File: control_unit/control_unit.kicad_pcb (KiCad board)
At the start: 2 copper layers, 100 x 95 mm, 111 parts, among them J1 Conn_02x03_Counter_Clockwise, J2 Conn_01x02_Socket, J4 SERVO_PWM, J5 BLDC1, J6 BLDC1, J7 BLDC1, J8 BLDC1, J9 Barrel_Jack_Switch, M1 Motor_Servo, M2 Fan, Q3 2N7002, Q4 MMBT5551L, Q7 AO3400A, Q8 AO3400A, U14 MCP2515-xSO, U15 BNO055 DIP, U3 ATA6561-GAQW-N, U4 ADS1015IDGS, X1 16MHz

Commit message: control_unit Rev00発注
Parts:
- added G***: LOGO, myfootprint:aqua_logo, F.Cu at (167.5, 69.8)
- added LED2: GREEN, LED_SMD:LED_0805_2012Metric, F.Cu at (130.5, 115.2)
- added R16: 1.2k, Resistor_SMD:R_0603_1608Metric, F.Cu at (130.5, 119.6)
- Analog_IN1: footprint Connector_JST:JST_XH_B4B-XH-AM_1x04_P2.50mm_Vertical -> Connector_JST:JST_XA_B04B-XASK-1-A_1x04_P2.50mm_Vertical
- CAN1: footprint Connector_JST:JST_XH_B2B-XH-A_1x02_P2.50mm_Vertical -> Connector_JST:JST_XA_B02B-XASK-1-A_1x02_P2.50mm_Vertical
- D2: value ~ -> SS54
- J4: footprint Connector_JST:JST_XH_B4B-XH-A_1x04_P2.50mm_Vertical -> Connector_JST:JST_XA_B04B-XASK-1-A_1x04_P2.50mm_Vertical
- LED1, LED_BNO1, LED_ESC_1, LED_ESC_2, LED_ESC_3, LED_ESC_4: footprint LED_SMD:LED_1206_3216Metric -> LED_SMD:LED_0805_2012Metric
- moved C1 24.5 mm to (98.0, 76.1)
- moved C2 24.5 mm to (152.0, 77.1)
- moved C5 24.5 mm to (137.6, 89.7)
- moved CAN2 24.5 mm to (91.8, 96.6)
- moved Cbst1 24.5 mm to (120.4, 109.3)
- moved Cc1 24.5 mm to (109.3, 107.6)
- moved Cc2 24.5 mm to (109.3, 109.6)
- moved Cc3 24.5 mm to (104.8, 111.8)
- moved Cin1 24.5 mm to (95.0, 124.1)
- moved Cin10 24.5 mm to (105.5, 133.6)
- moved Cin11 24.5 mm to (109.0, 133.6)
- moved Cin12 24.5 mm to (112.5, 133.6)
- moved Cin2 24.5 mm to (98.5, 124.1)
- moved Cin3 24.5 mm to (102.5, 121.6)
- moved Cin4 24.5 mm to (106.0, 121.6)
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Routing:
- net Net-(U14-OSC2): track 19.9 -> 10.1 mm
- net +5.1V: track 216.1 -> 221.8 mm, vias 16 -> 24
- net Net-(LED2-A): track 0.00 -> 2.17 mm
- net Net-(J1-Pin_5): track 36.6 -> 34.8 mm
- net +24V: track 28.5 -> 27.2 mm
- net SERVO4: track 28.4 -> 27.3 mm
- net Net-(U5-SS/TRK): track 6.99 -> 6.02 mm
- net Net-(LED_ESC_3-A): track 3.26 -> 2.38 mm
- net Net-(LED_ESC_2-A): track 3.26 -> 2.46 mm
- net Net-(LED_ESC_4-A): track 3.39 -> 2.71 mm
- net Net-(LED_ESC_1-A): track 3.14 -> 2.46 mm
- net Net-(U5-RT): track 5.47 -> 4.96 mm
- net GND: vias 116 -> 193
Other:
- outline, holes or cut-outs redrawn
- board text added: "AIN1"
- board text added: "AIN2"
- board text added: "AIN3"
- board text added: "AIN4"
- board text added: "REV01"
- board text added: "SERVO1"
- board text added: "SERVO2"
- board text added: "SERVO3"
- board text added: "SERVO4"

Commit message: 制御基板のファイル整理と微調整
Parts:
- removed J1: Conn_02x03_Counter_Clockwise, Connector_PinHeader_2.54mm:PinHeader_2x03_P2.54mm_Vertical
- added headlight1: Conn_02x03_Odd_Even, Connector_PinHeader_2.54mm:PinHeader_2x03_P2.54mm_Vertical, F.Cu at (166.5, 128.8)
- LED1, LED_ESC_1, LED_ESC_2, LED_ESC_3, LED_ESC_4: value GREEN -> RED
- R11: value 10kΩ -> 10k
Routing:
- net +5.1V: track 221.8 -> 220.9 mm
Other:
- board text added: "5.1"
- board text added: "HB_A"
- board text added: "HB_K"
- board text added: "IR"
- board text added: "LB"
- board text added: "NC"

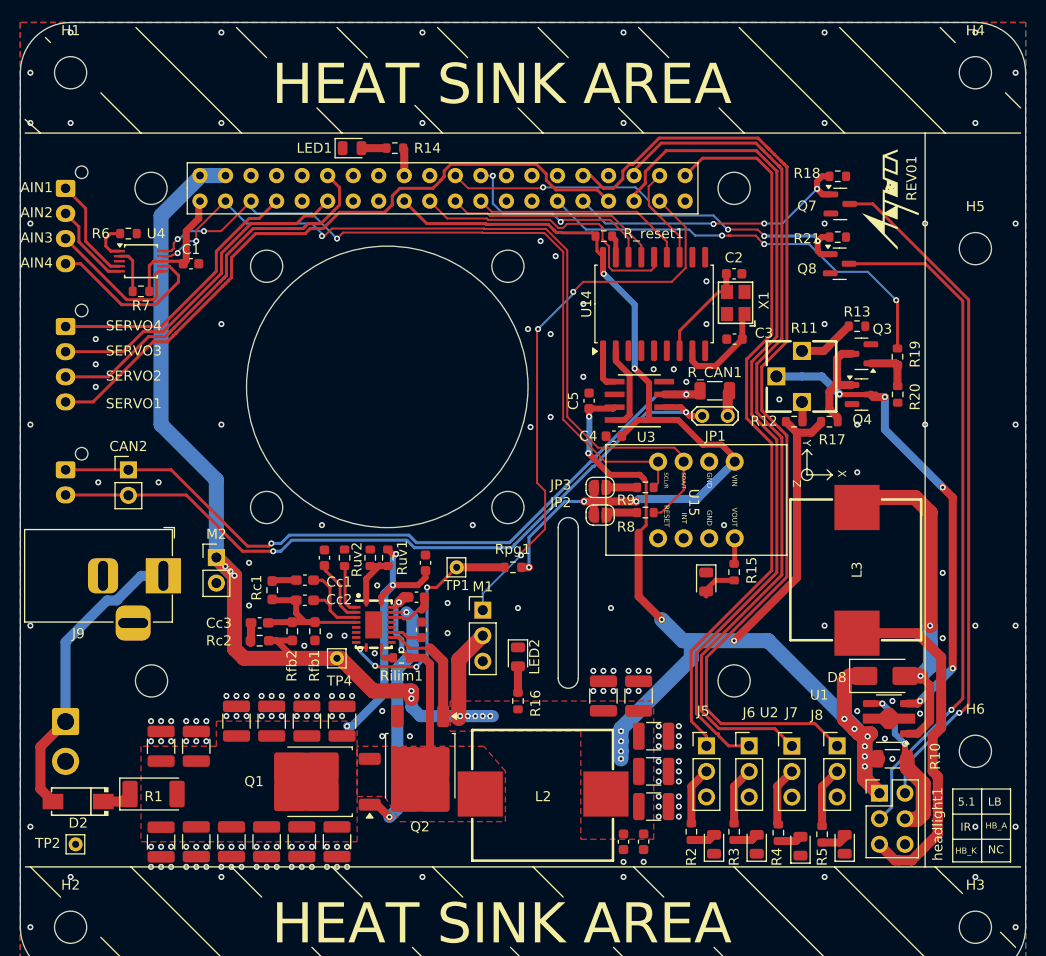
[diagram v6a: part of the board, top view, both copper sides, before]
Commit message: 基板防水(LAN)作成開始
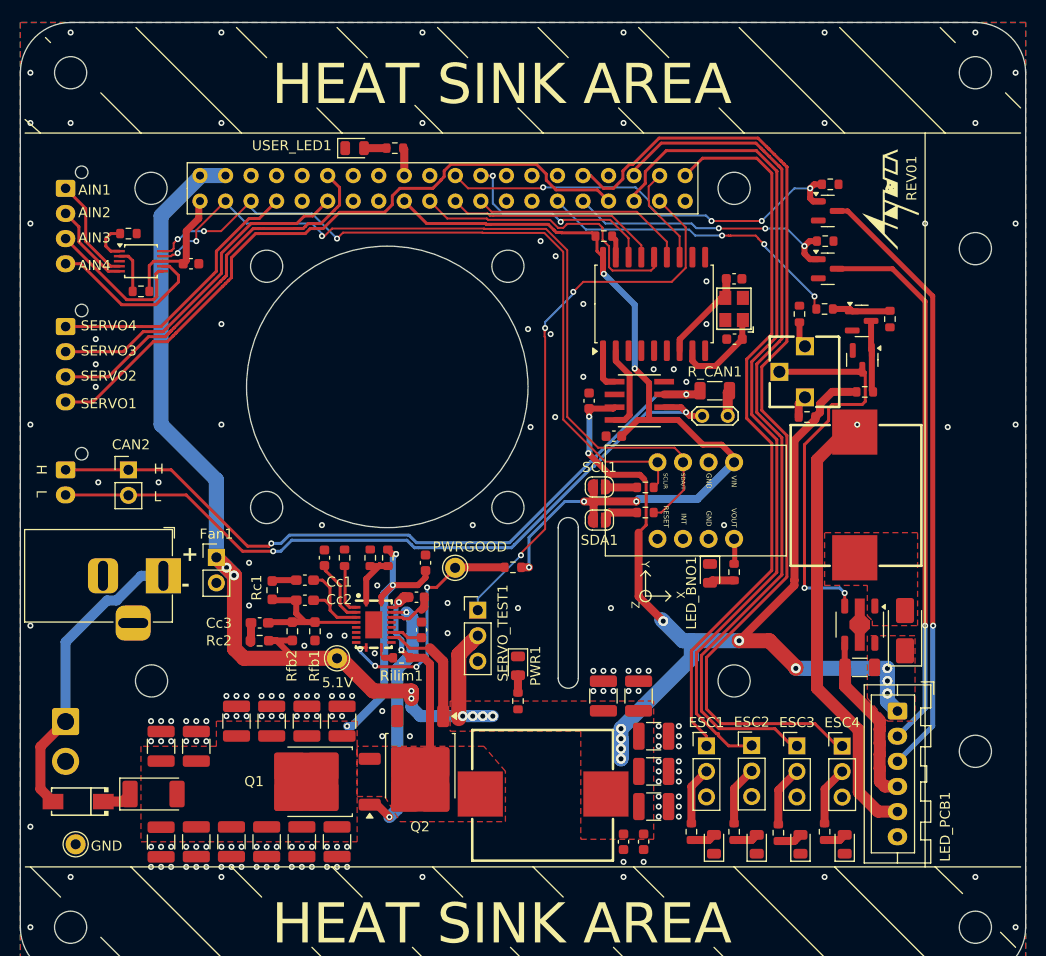
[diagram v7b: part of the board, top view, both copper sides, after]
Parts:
- removed J5, J6, J7, J8: BLDC1, Connector_PinHeader_2.54mm:PinHeader_1x03_P2.54mm_Vertical
- removed JP2, JP3: SolderJumper_2_Open, Jumper:SolderJumper-2_P1.3mm_Open_RoundedPad1.0x1.5mm
- removed LED1: RED, LED_SMD:LED_0805_2012Metric
- removed LED2: GREEN, LED_SMD:LED_0805_2012Metric
- removed M1: Motor_Servo, Connector_PinHeader_2.54mm:PinHeader_1x03_P2.54mm_Vertical
- removed M2: Fan, Connector_PinHeader_2.54mm:PinHeader_1x02_P2.54mm_Vertical
- removed headlight1: Conn_02x03_Odd_Even, Connector_PinHeader_2.54mm:PinHeader_2x03_P2.54mm_Vertical
- added ESC1: ~, Connector_PinHeader_2.54mm:PinHeader_1x03_P2.54mm_Vertical, F.Cu at (149.3, 124.1)
- added ESC2: ~, Connector_PinHeader_2.54mm:PinHeader_1x03_P2.54mm_Vertical, F.Cu at (153.8, 124.0)
- added ESC3: ~, Connector_PinHeader_2.54mm:PinHeader_1x03_P2.54mm_Vertical, F.Cu at (158.3, 124.1)
- added ESC4: ~, Connector_PinHeader_2.54mm:PinHeader_1x03_P2.54mm_Vertical, F.Cu at (162.8, 124.1)
- added Fan1: Fan, Connector_PinHeader_2.54mm:PinHeader_1x02_P2.54mm_Vertical, F.Cu at (100.5, 105.3)
- added LED_PCB1: Conn_01x06_Pin, Connector_JST:JST_XA_B06B-XASK-1_1x06_P2.50mm_Vertical, F.Cu at (168.3, 120.6)
- added PWR1: GREEN, LED_SMD:LED_0805_2012Metric, F.Cu at (130.5, 116.1)
- added SCL1: SolderJumper_2_Open, Jumper:SolderJumper-2_P1.3mm_Open_RoundedPad1.0x1.5mm, F.Cu at (138.6, 98.3)
- added SDA1: SolderJumper_2_Open, Jumper:SolderJumper-2_P1.3mm_Open_RoundedPad1.0x1.5mm, F.Cu at (138.6, 101.6)
- added SERVO_TEST1: Motor_Servo, Connector_PinHeader_2.54mm:PinHeader_1x03_P2.54mm_Vertical, F.Cu at (126.5, 110.6)
- added USER_LED1: RED, LED_SMD:LED_0805_2012Metric, F.Cu at (114.3, 64.6)
- R17: value 10k -> 1k
- TP1, TP2, TP4: footprint Connector_Pin:Pin_D0.7mm_L6.5mm_W1.8mm_FlatFork -> Connector_Pin:Pin_D1.0mm_L10.0mm
- U1: value ~ -> CL6808
- moved U1 9.79 mm to (164.5, 112.0), turned to -90 degrees
- moved R10 9.66 mm to (164.5, 116.2), turned to 180 degrees
- moved R19 8.67 mm to (161.0, 80.6), turned to 180 degrees
- moved R20 7.54 mm to (167.5, 81.6)
- moved L3 7.50 mm to (164.0, 99.1), turned to 90 degrees
- moved Q7 6.57 mm to (161.3, 76.6)
- moved R18 6.57 mm to (161.1, 73.8)
- moved R13 5.86 mm to (158.5, 81.1), turned to 90 degrees
- moved Q8 5.38 mm to (161.3, 70.8)
- moved R21 5.30 mm to (161.6, 68.2)
- moved D8 4.92 mm to (169.0, 112.6), turned to 90 degrees
- moved R17 4.60 mm to (165.0, 88.8)
- moved Q3 3.45 mm to (164.8, 85.7), turned to -90 degrees
- moved Q4 3.27 mm to (164.7, 81.8), turned to 0 degrees
- moved R12 1.35 mm to (159.3, 91.3), turned to 180 degrees
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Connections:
- net BATTERY_OK renamed USER_LED
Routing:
- net Net-(D8-A): track 32.5 -> 0.00 mm, vias 2 -> 0
- net +5.1V: track 220.9 -> 205.6 mm, vias 24 -> 20
- net Net-(LED_PCB1-Pin_2): track 67.7 -> 54.5 mm
- net HighBeam: track 42.7 -> 31.0 mm
- net Net-(LED_PCB1-Pin_5): track 34.8 -> 44.2 mm
- net Net-(Q3-D): track 47.3 -> 40.0 mm, vias 5 -> 2
- net Net-(LED_PCB1-Pin_3): track 67.8 -> 60.8 mm
- net Net-(R11-Pad3): track 5.67 -> 2.61 mm
- net Net-(Q3-G): track 9.64 -> 7.15 mm
- net LowBeam: track 29.5 -> 27.7 mm
- net Net-(LED_PCB1-Pin_4): track 15.9 -> 17.2 mm, vias 2 -> 0
- net Net-(LED_BNO1-A): track 3.78 -> 2.50 mm
- net Net-(Q4-B): track 4.82 -> 5.80 mm
- net Net-(U14-OSC2): track 10.1 -> 9.31 mm
- net Net-(U14-OSC1): track 9.90 -> 9.23 mm
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- added copper zone on F.Cu, net Net-(D8-A)
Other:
- board text added: "+"
- board text added: "-"
- board text added: "5.1V"
- board text added: "GND"
- board text added: "H"
- board text added: "L"
- board text added: "PWRGOOD"
- board text removed: "5.1"
- board text removed: "HB_A"
- board text removed: "HB_K"
- board text removed: "IR"
- board text removed: "LB"
- board text removed: "NC"

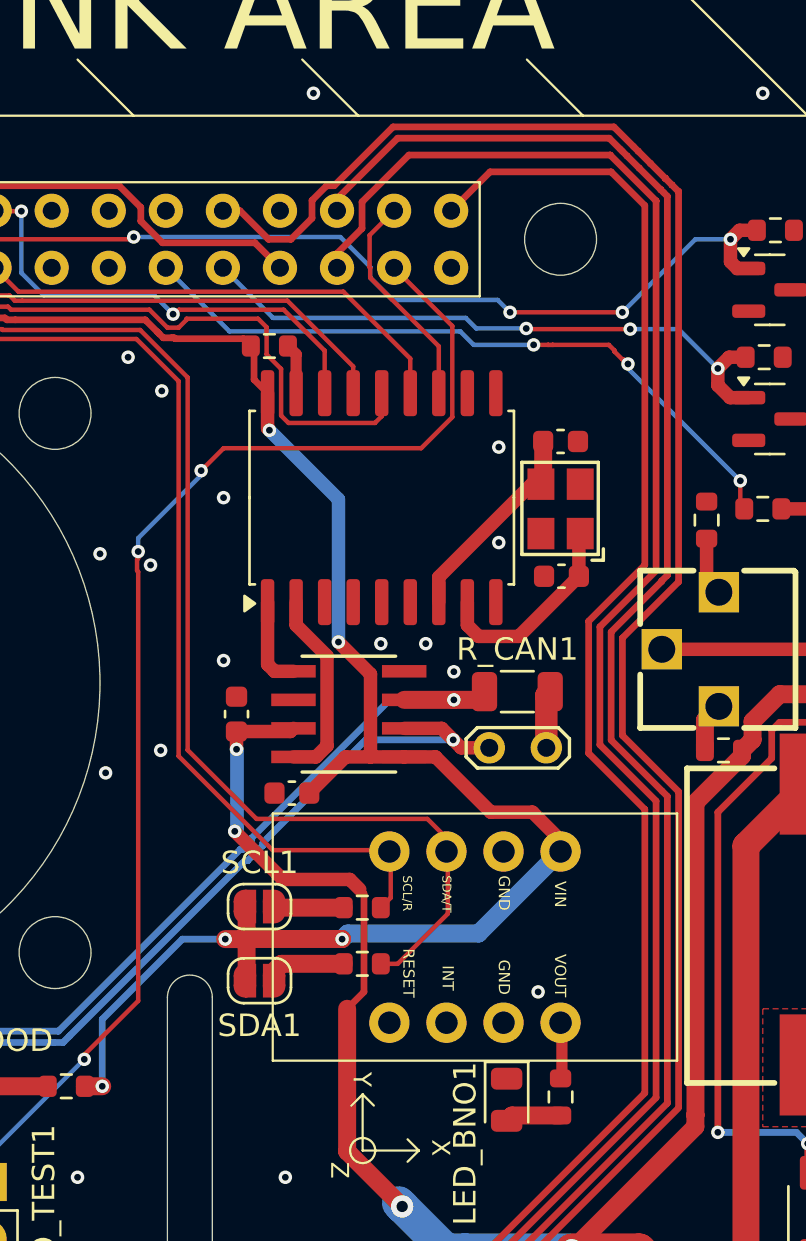
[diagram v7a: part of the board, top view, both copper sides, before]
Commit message: AQUA_VESC REV01作成
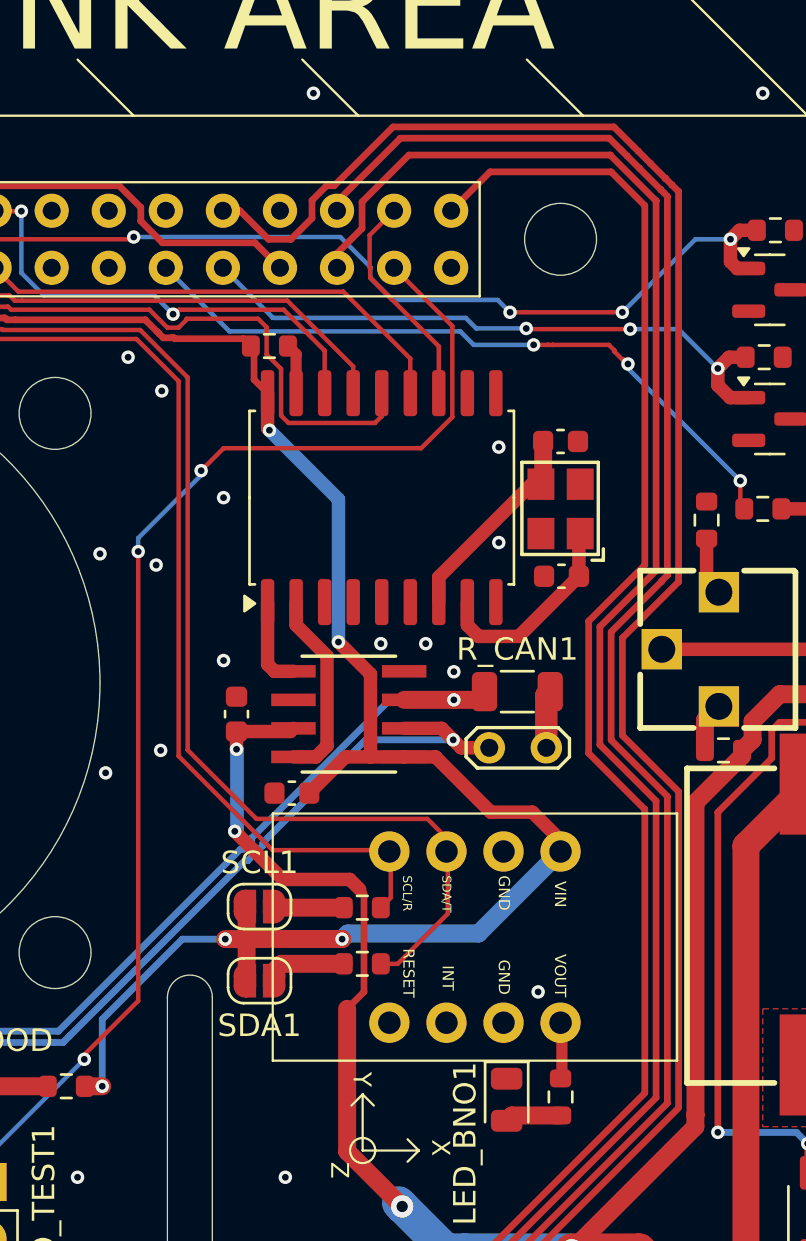
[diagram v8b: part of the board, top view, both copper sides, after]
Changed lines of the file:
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@@
 			(psa4output no)
 			(plot_black_and_white yes)
-			(plotinvisibletext no)
 			(sketchpadsonfab no)
 			(plotpadnumbers no)
@@
 	)
 	(via
-		(at 133.775995 83.099005)
+		(at 134.025995 83.099005)
 		(size 0.6)
 		(drill 0.3)
@@
 	)
 	(segment
-		(start 133.174995 82.850062)
-		(end 133.174995 83.347948)
+		(start 130.825995 104.899005)
+		(end 130.825995 105.099005)
 		(width 0.2)
 		(layer "F.Cu")
@@
 	)
 	(segment
-		(start 133.174995 83.347948)
-		(end 133.225995 83.398948)
+		(start 133.225995 82.499005)
+		(end 133.225995 102.499005)
 		(width 0.2)
 		(layer "F.Cu")
@@
 	)
 	(segment
-		(start 133.225995 82.499005)
-		(end 133.225995 82.799062)
+		(start 133.225995 102.499005)
+		(end 130.825995 104.899005)
 		(width 0.2)
 		(layer "F.Cu")
@@
 	)
 	(segment
-		(start 130.825995 104.899005)
-		(end 130.825995 105.099005)
-		(width 0.2)
-		(layer "F.Cu")
-		(net 34)
-	)
-	(segment
 		(start 147.206995 76.514973)
 		(end 147.206995 72.460005)
@@
 	)
 	(segment
-		(start 133.225995 82.799062)
-		(end 133.174995 82.850062)
-		(width 0.2)
-		(layer "F.Cu")
-		(net 34)
-	)
-	(segment
 		(start 136.026995 78.899005)
 		(end 137.026995 77.899005)
@@
 	)
 	(segment
-		(start 133.225995 83.398948)
-		(end 133.225995 102.499005)
-		(width 0.2)
-		(layer "F.Cu")
-		(net 34)
-	)
-	(segment
-		(start 133.225995 102.499005)
-		(end 130.825995 104.899005)
-		(width 0.2)
-		(layer "F.Cu")
-		(net 34)
-	)
-	(segment
 		(start 137.026995 77.899005)
 		(end 145.822963 77.899005)
@@
 	)
 	(segment
-		(start 155.525995 65.431962)
-		(end 154.984517 64.890484)
+		(start 154.984517 64.890483)
+		(end 154.779183 64.685151)
 		(width 0.3)
 		(layer "F.Cu")
@@
 	)
 	(segment
-		(start 156.611854 66.517821)
-		(end 156.484515 66.390484)
-		(width 0.3)
-		(layer "F.Cu")
-		(net 43)
-	)
-	(segment
-		(start 154.691038 64.597004)
-		(end 154.193038 64.099005)
+		(start 156.777995 83.555526)
+		(end 156.777995 66.683963)
 		(width 0.3)
 		(layer "F.Cu")
@@
 	)
 	(segment
-		(start 157.800995 124.074005)
-		(end 156.075995 122.349005)
+		(start 156.777995 83.555525)
+		(end 156.777995 83.555526)
 		(width 0.3)
 		(layer "F.Cu")
@@
 	)
 	(segment
-		(start 156.484515 66.390484)
-		(end 156.483516 66.389483)
+		(start 157.775995 124.074005)
+		(end 157.800995 124.074005)
 		(width 0.3)
 		(layer "F.Cu")
@@
 	)
 	(segment
-		(start 154.984517 64.890483)
-		(end 154.779183 64.685151)
+		(start 156.483516 66.389483)
+		(end 156.483517 66.389483)
 		(width 0.3)
 		(layer "F.Cu")
@@
 	)
 	(segment
-		(start 156.548734 93.163224)
-		(end 154.276995 90.891485)
+		(start 156.777995 66.683963)
+		(end 156.611854 66.517821)
 		(width 0.3)
 		(layer "F.Cu")
@@
 	)
 	(segment
-		(start 157.775995 124.074005)
-		(end 157.800995 124.074005)
+		(start 157.800995 124.074005)
+		(end 156.075995 122.349005)
 		(width 0.3)
 		(layer "F.Cu")
@@
 	)
 	(segment
-		(start 154.779183 64.685151)
-		(end 154.691038 64.597004)
+		(start 144.900995 64.099005)
+		(end 142.075995 66.924005)
 		(width 0.3)
 		(layer "F.Cu")
@@
 	)
 	(segment
-		(start 154.276995 90.891485)
-		(end 154.276995 86.077265)
+		(start 155.525995 65.431964)
+		(end 155.525995 65.431962)
 		(width 0.3)
 		(layer "F.Cu")
@@
 	)
 	(segment
-		(start 156.525995 83.828265)
-		(end 156.525995 83.807525)
+		(start 156.777995 93.392485)
+		(end 154.276995 90.891485)
 		(width 0.3)
 		(layer "F.Cu")
@@
 	)
 	(segment
-		(start 156.075995 122.349005)
-		(end 150.525995 122.349005)
+		(start 154.276995 86.077265)
+		(end 156.525995 83.828265)
 		(width 0.3)
 		(layer "F.Cu")
@@
 	)
 	(segment
-		(start 156.777995 93.392485)
-		(end 156.548734 93.163224)
+		(start 156.611854 66.517821)
+		(end 156.484515 66.390484)
 		(width 0.3)
 		(layer "F.Cu")
@@
 	)
 	(segment
-		(start 156.525995 83.807525)
-		(end 156.777995 83.555525)
+		(start 154.779183 64.685151)
+		(end 154.691038 64.597004)
 		(width 0.3)
 		(layer "F.Cu")
@@
 	(segment
 		(start 156.777995 107.055525)
-		(end 156.777995 107.014047)
-		(width 0.3)
-		(layer "F.Cu")
-		(net 43)
-	)
-	(segment
-		(start 155.525995 65.431964)
-		(end 155.525995 65.431962)
+		(end 156.777995 93.392485)
 		(width 0.3)
 		(layer "F.Cu")
@@
 	)
 	(segment
-		(start 148.777995 120.601005)
-		(end 148.777995 115.055525)
+		(start 155.525995 65.431962)
+		(end 154.984517 64.890484)
 		(width 0.3)
 		(layer "F.Cu")
@@
 	)
 	(segment
-		(start 156.777995 66.683963)
-		(end 156.611854 66.517821)
+		(start 156.525995 83.807525)
+		(end 156.777995 83.555525)
 		(width 0.3)
 		(layer "F.Cu")
@@
 	)
 	(segment
-		(start 154.984517 64.890484)
-		(end 154.984517 64.890483)
+		(start 150.525995 122.349005)
+		(end 148.777995 120.601005)
 		(width 0.3)
 		(layer "F.Cu")
@@
 	)
 	(segment
-		(start 156.483517 66.389483)
-		(end 155.525995 65.431964)
+		(start 156.075995 122.349005)
+		(end 150.525995 122.349005)
 		(width 0.3)
 		(layer "F.Cu")
@@
 	)
 	(segment
-		(start 156.777995 107.014047)
-		(end 156.777995 93.392485)
+		(start 156.525995 83.828265)
+		(end 156.525995 83.807525)
 		(width 0.3)
 		(layer "F.Cu")
@@
 	)
 	(segment
-		(start 156.483516 66.389483)
-		(end 156.483517 66.389483)
+		(start 156.484515 66.390484)
+		(end 156.483516 66.389483)
 		(width 0.3)
 		(layer "F.Cu")
@@
 	)
 	(segment
-		(start 154.276995 86.077265)
-		(end 156.525995 83.828265)
+		(start 142.075995 66.924005)
+		(end 142.075995 67.329005)
 		(width 0.3)
 		(layer "F.Cu")
@@
 	)
 	(segment
-		(start 144.775995 64.099005)
-		(end 142.075995 66.799005)
+		(start 154.691038 64.597004)
+		(end 154.193038 64.099005)
 		(width 0.3)
 		(layer "F.Cu")
@@
 	)
 	(segment
-		(start 154.193038 64.099005)
-		(end 144.775995 64.099005)
+		(start 148.777995 120.601005)
+		(end 148.777995 115.055525)
 		(width 0.3)
 		(layer "F.Cu")
@@
 	)
 	(segment
-		(start 156.777995 83.555526)
-		(end 156.777995 66.683963)
+		(start 156.483517 66.389483)
+		(end 155.525995 65.431964)
 		(width 0.3)
 		(layer "F.Cu")
@@
 	)
 	(segment
-		(start 150.525995 122.349005)
-		(end 148.777995 120.601005)
+		(start 154.276995 90.891485)
+		(end 154.276995 86.077265)
 		(width 0.3)
 		(layer "F.Cu")
@@
 	)
 	(segment
-		(start 142.075995 66.799005)
-		(end 142.075995 67.329005)
+		(start 154.193038 64.099005)
+		(end 144.900995 64.099005)
 		(width 0.3)
 		(layer "F.Cu")
@@
 	)
 	(segment
-		(start 156.777995 83.555525)
-		(end 156.777995 83.555526)
+		(start 154.984517 64.890484)
+		(end 154.984517 64.890483)
 		(width 0.3)
 		(layer "F.Cu")
